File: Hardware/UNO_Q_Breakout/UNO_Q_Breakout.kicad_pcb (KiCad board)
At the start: 2 copper layers, 15.5 x 41 mm, 3 parts, among them J1 Conn_02x30_Odd_Even, J2 LAMP1

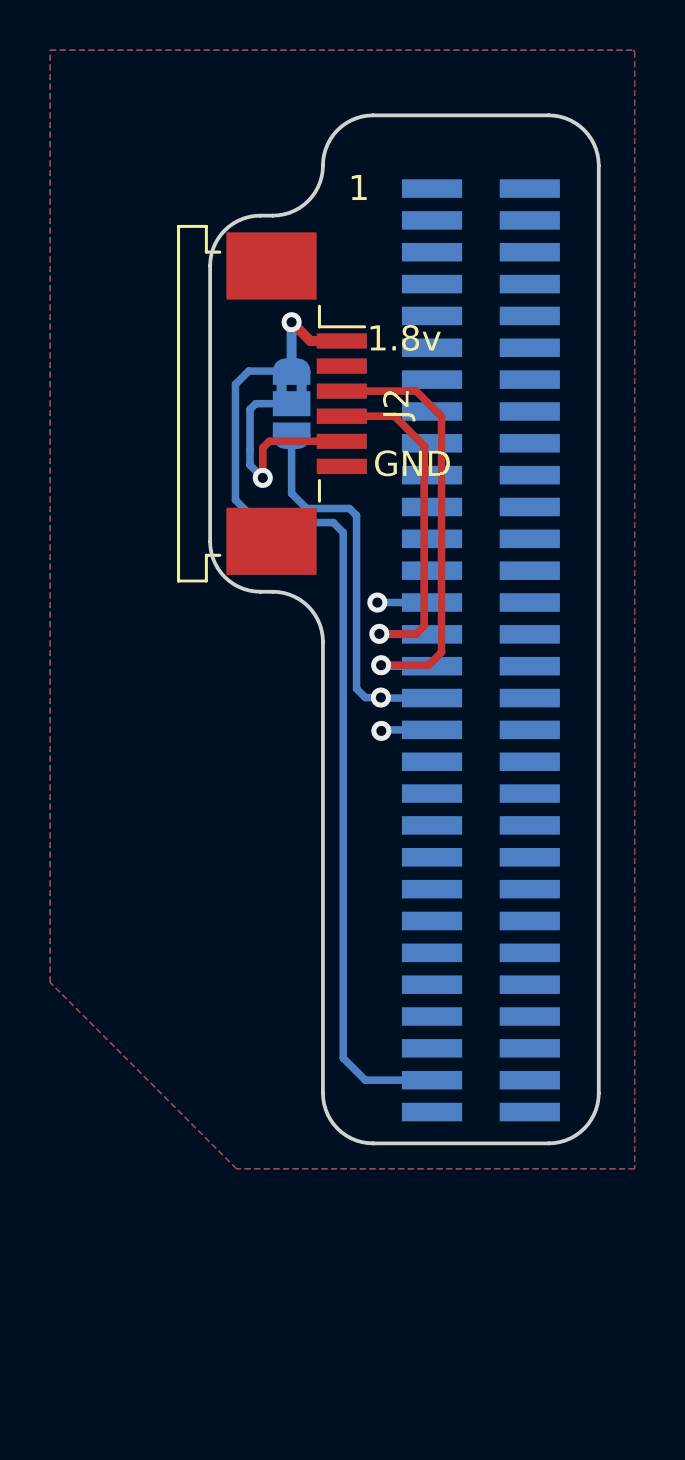
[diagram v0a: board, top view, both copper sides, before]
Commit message: Add labels to breackout
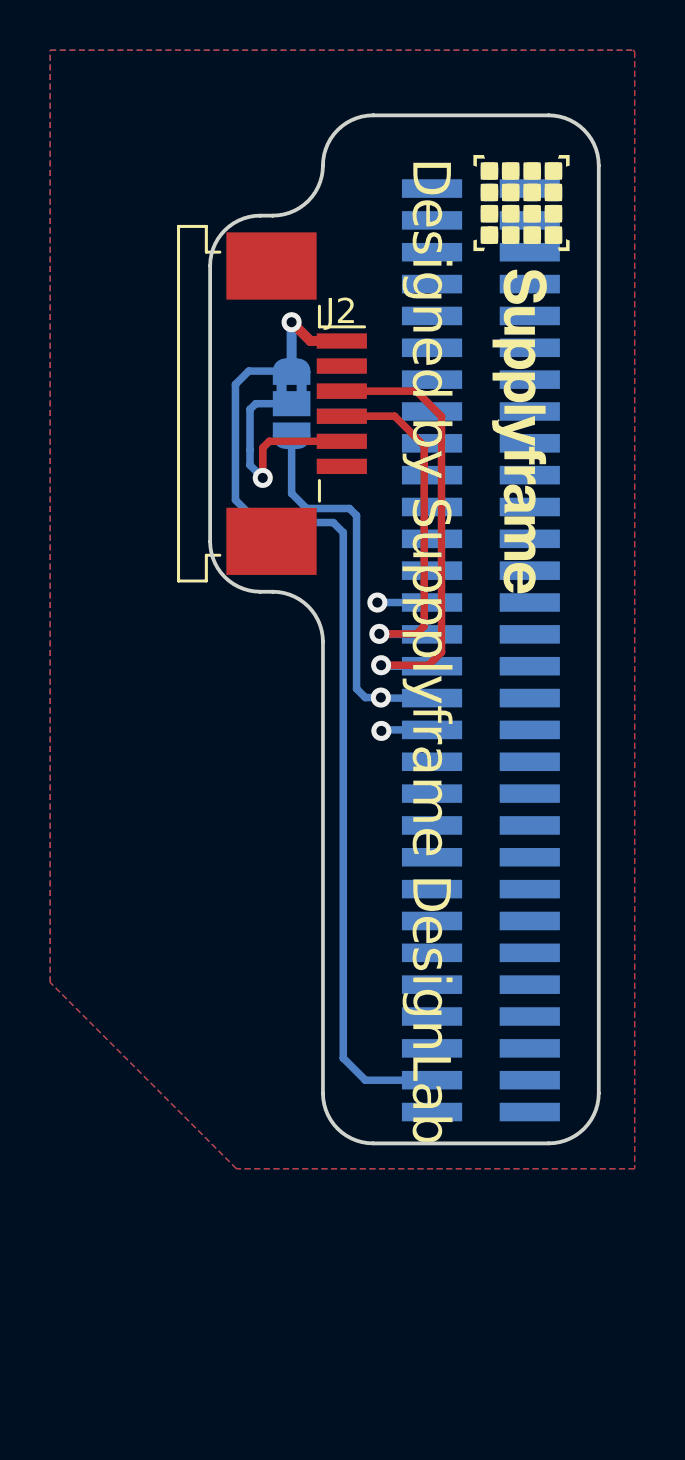
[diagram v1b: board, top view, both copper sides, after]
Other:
- board text added: "Designed by Suppplyframe DesignLab"
- board text removed: "1.8v"
